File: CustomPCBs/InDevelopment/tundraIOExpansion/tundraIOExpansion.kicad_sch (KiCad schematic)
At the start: 35 parts, among them J1 Conn_01x25, J2 Conn_ARM_SWD_TagConnect_TC203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, U1 RP2040, U2 MX25L3233FM2, Y1 Crystal, Y2 32.768kHz

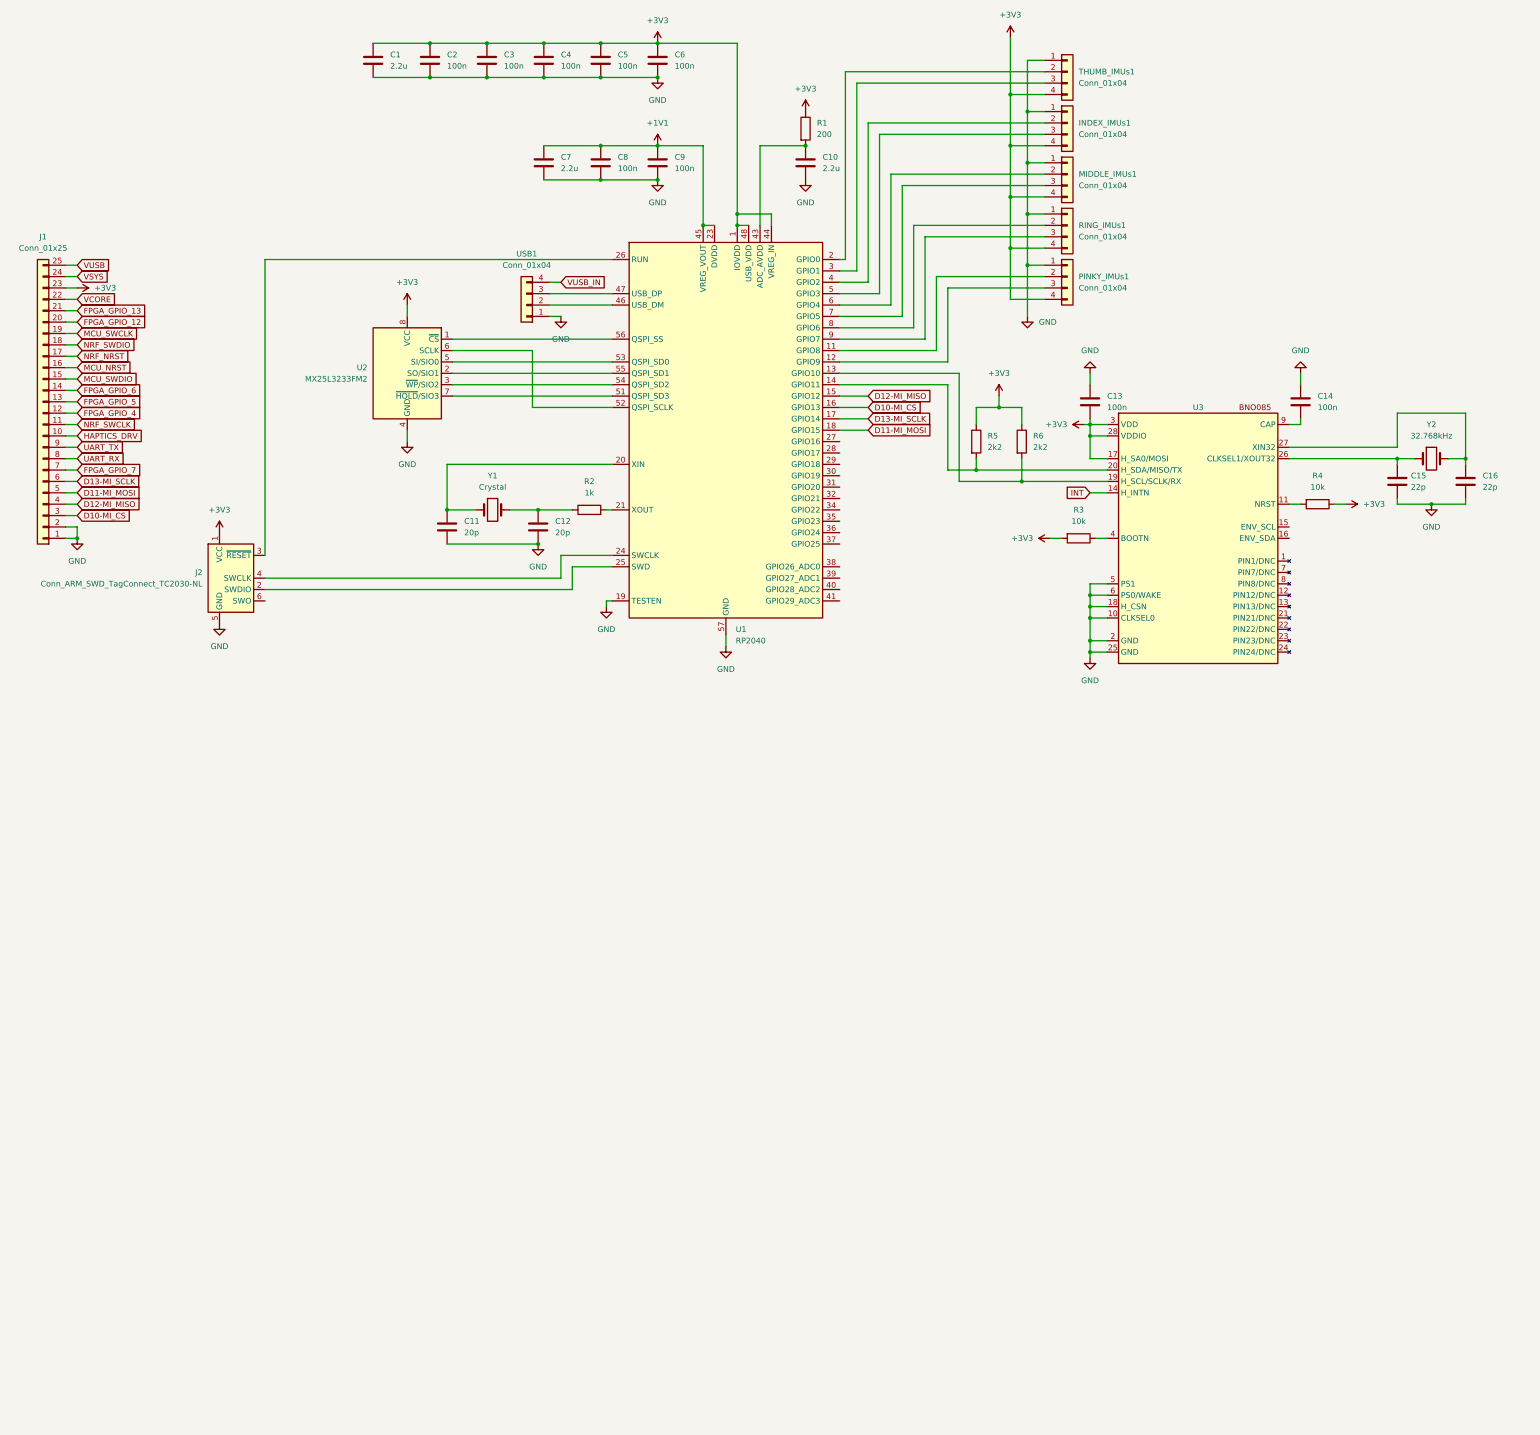
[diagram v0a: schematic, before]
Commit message: Adding variant for BNO 0x4A and 0x4B addresses
Also cleaned up the folder structure and changed schematic for the
custom Tundra expansion board
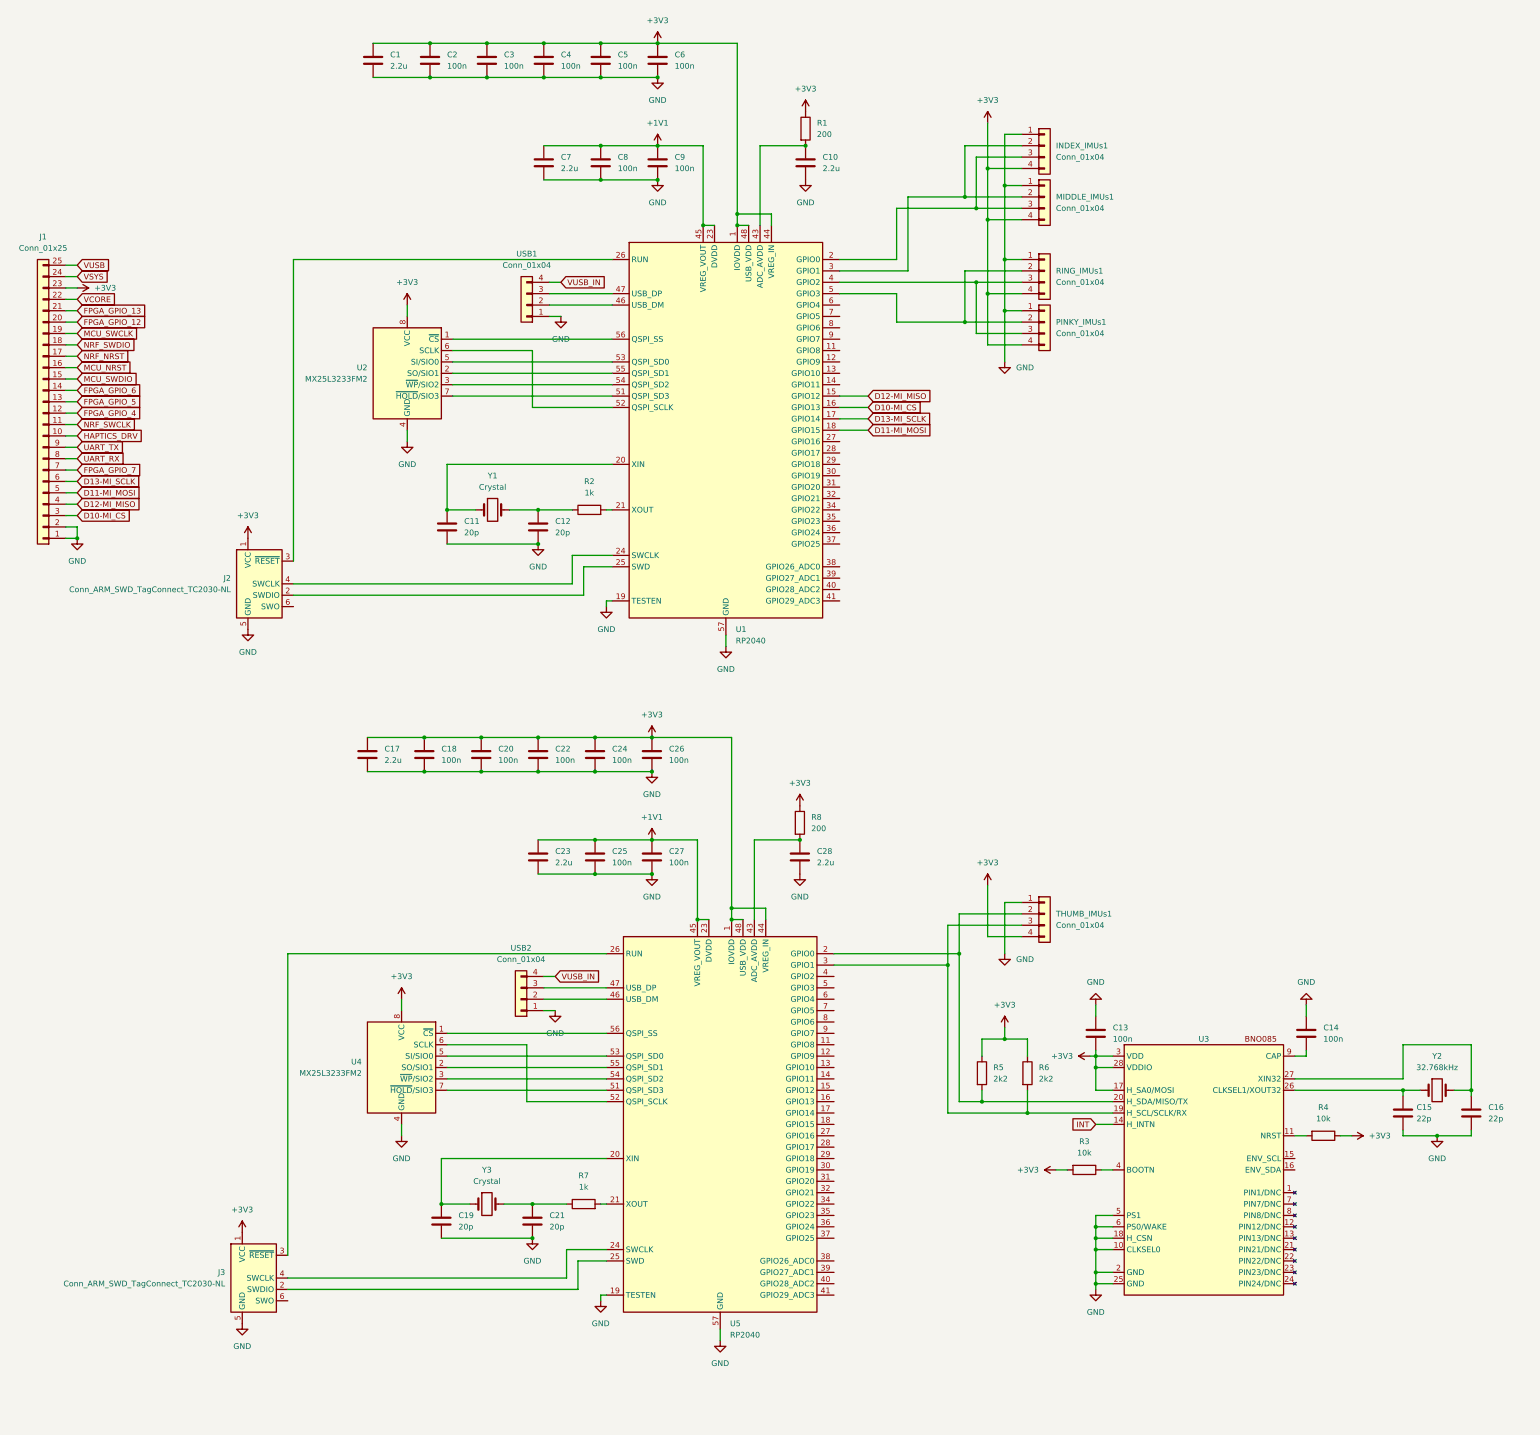
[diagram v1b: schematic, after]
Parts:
- added C17, C23, C28: 2.2u, Capacitor_SMD:C_0603_1608Metric, symbol Device:C
- added C18, C20, C22, C24, C25, C26, C27: 100n, Capacitor_SMD:C_0603_1608Metric, symbol Device:C
- added C19, C21: 20p, Capacitor_SMD:C_0603_1608Metric, symbol Device:C
- added J3: Conn_ARM_SWD_TagConnect_TC2030-NL, Connector:Tag-Connect_TC2030-IDC-NL_2x03_P1.27mm_Vertical, symbol Connector:Conn_ARM_SWD_TagConnect_TC2030-NL
- added R7: 1k, Resistor_SMD:R_0603_1608Metric, symbol Device:R
- added R8: 200, Resistor_SMD:R_0603_1608Metric, symbol Device:R
- added U4: MX25L3233FM2, Package_SO:SOP-8_5.28x5.23mm_P1.27mm, symbol Memory_Flash:MX25L3233FM2
- added U5: RP2040, Package_DFN_QFN:QFN-56-1EP_7x7mm_P0.4mm_EP3.2x3.2mm, symbol MCU_RaspberryPi:RP2040
- added USB2: Conn_01x04, Connector_JST:JST_SH_SM04B-SRSS-TB_1x04-1MP_P1.00mm_Horizontal, symbol Connector_Generic:Conn_01x04
- added Y3: Crystal, Crystal:Crystal_SMD_HC49-SD, symbol Device:Crystal
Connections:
- net +1V1: now also C23.1, C25.1, C27.1, U5.23 (DVDD), U5.45 (VREG_VOUT), U5.50 (DVDD)
- net +3V3: now also C17.1, C18.1, C20.1, C22.1, C24.1, C26.1, J3.1 (VCC), R8.1, U4.8 (VCC), U5.1 (IOVDD), U5.10 (IOVDD), U5.22 (IOVDD), U5.33 (IOVDD), U5.42 (IOVDD), U5.44 (VREG_IN), U5.48 (USB_VDD), U5.49 (IOVDD)
- net GND: now also C17.2, C18.2, C19.2, C20.2, C21.2, C22.2, C23.2, C24.2, C25.2, C26.2, C27.2, C28.2, J3.5 (GND), U4.4 (GND), U5.19 (TESTEN), U5.57 (GND), USB2.1 (Pin_1)
- net VUSB_IN: now also USB2.4 (Pin_4)
- net at R5.2, U3.20 (H_SDA/MISO/TX): now also THUMB_IMUs1.2 (Pin_2), U5.2 (GPIO0); no longer U1.14 (GPIO11)
- net at U1.11 (GPIO8): no longer PINKY_IMUs1.2 (Pin_2)
- net at U1.12 (GPIO9): no longer PINKY_IMUs1.3 (Pin_3)
- net at R6.2, U3.19 (H_SCL/SCLK/RX): now also THUMB_IMUs1.3 (Pin_3), U5.3 (GPIO1); no longer U1.13 (GPIO10)
- net at U1.2 (GPIO0): now also INDEX_IMUs1.3 (Pin_3), MIDDLE_IMUs1.3 (Pin_3); no longer THUMB_IMUs1.2 (Pin_2)
- net at U1.3 (GPIO1): now also INDEX_IMUs1.2 (Pin_2), MIDDLE_IMUs1.2 (Pin_2); no longer THUMB_IMUs1.3 (Pin_3)
- net at U1.4 (GPIO2): now also PINKY_IMUs1.3 (Pin_3), RING_IMUs1.3 (Pin_3); no longer INDEX_IMUs1.2 (Pin_2)
- net at U1.5 (GPIO3): now also PINKY_IMUs1.2 (Pin_2), RING_IMUs1.2 (Pin_2); no longer INDEX_IMUs1.3 (Pin_3)
- net at U1.6 (GPIO4): no longer MIDDLE_IMUs1.2 (Pin_2)
- net at U1.7 (GPIO5): no longer MIDDLE_IMUs1.3 (Pin_3)
- net at U1.8 (GPIO6): no longer RING_IMUs1.2 (Pin_2)
- net at U1.9 (GPIO7): no longer RING_IMUs1.3 (Pin_3)
- new net: J3.2 (SWDIO), U5.25 (SWD)
- new net: J3.3 (~{RESET}), U5.26 (RUN)
- new net: J3.4 (SWCLK), U5.24 (SWCLK)
- new net: C21.1, R7.1, Y3.2
- new net: R7.2, U5.21 (XOUT)
- new net: C19.1, U5.20 (XIN), Y3.1
- new net: C28.1, R8.2, U5.43 (ADC_AVDD)
- new net: U4.1 (~{CS}), U5.56 (QSPI_SS)
- new net: U4.2 (SO/SIO1), U5.55 (QSPI_SD1)
- new net: U4.3 (~{WP}/SIO2), U5.54 (QSPI_SD2)
- new net: U4.5 (SI/SIO0), U5.53 (QSPI_SD0)
- new net: U4.6 (SCLK), U5.52 (QSPI_SCLK)
- new net: U4.7 (~{HOLD}/SIO3), U5.51 (QSPI_SD3)
- new net: U5.46 (USB_DM), USB2.2 (Pin_2)
- new net: U5.47 (USB_DP), USB2.3 (Pin_3)
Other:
- moved on the sheet: C13, C14, C15, C16, INDEX_IMUs1, J2, MIDDLE_IMUs1, PINKY_IMUs1, R3, R4, R5, R6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

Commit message: Updating some footprints
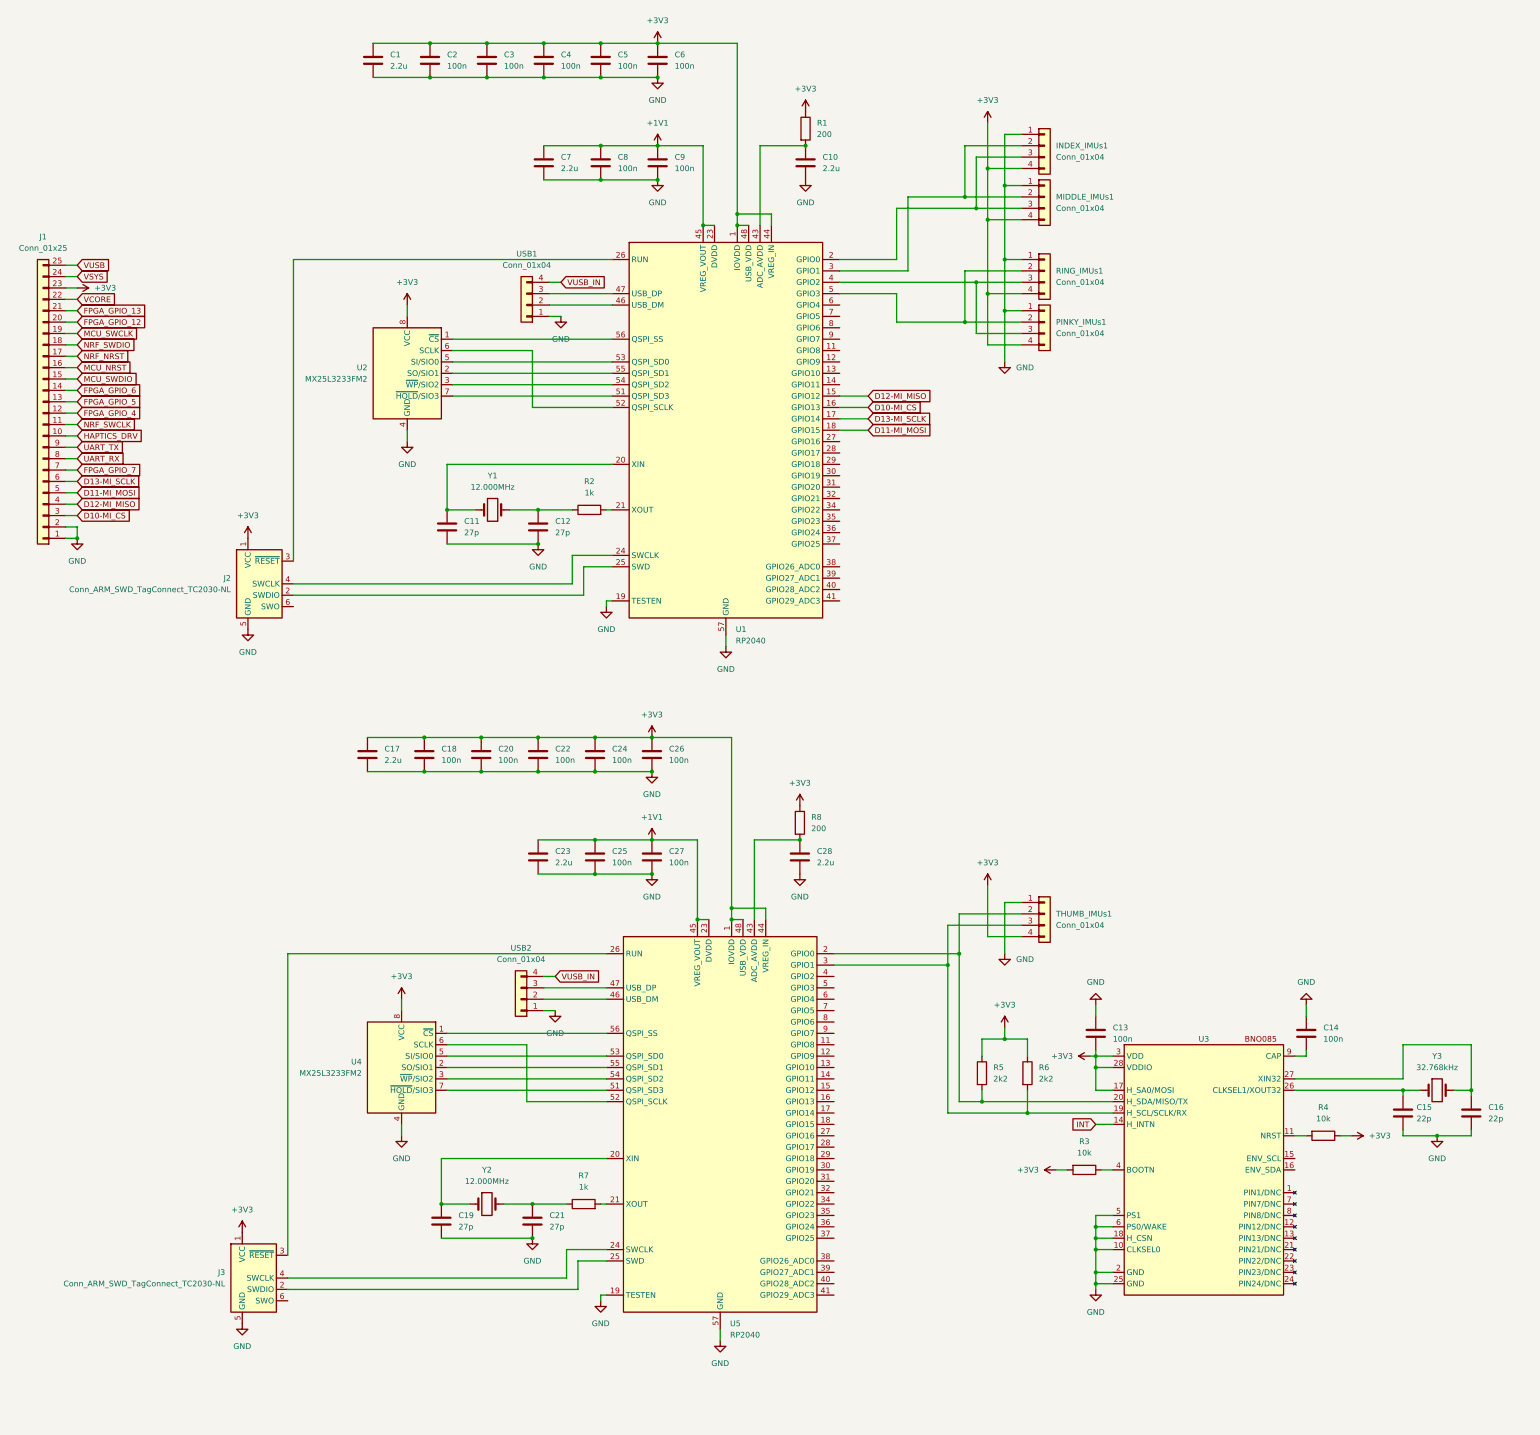
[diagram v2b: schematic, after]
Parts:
- removed Y3: Crystal, Crystal:Crystal_SMD_HC49-SD, symbol Device:Crystal
- added Y2: 12.000MHz, Crystal:Crystal_SMD_3225-4Pin_3.2x2.5mm, symbol Device:Crystal
- C1, C10, C13, C14, C15, C16, C17, C18, C2, C20, C22, C23, C24, C25, C26, C27, C28, C3, C4, C5, C6, C7, C8, C9: footprint Capacitor_SMD:C_0603_1608Metric -> Capacitor_SMD:C_0402_1005Metric
- C11, C12, C19, C21: value 20p -> 27p; footprint Capacitor_SMD:C_0603_1608Metric -> Capacitor_SMD:C_0402_1005Metric
- R1, R2, R3, R4, R5, R6, R7, R8: footprint Resistor_SMD:R_0603_1608Metric -> Resistor_SMD:R_0402_1005Metric
- Y1: value Crystal -> 12.000MHz; footprint Crystal:Crystal_SMD_HC49-SD -> Crystal:Crystal_SMD_3225-4Pin_3.2x2.5mm
- Y3: renamed from Y2; footprint Crystal:Crystal_SMD_3215-2Pin_3.2x1.5mm -> Crystal:Crystal_SMD_2012-2Pin_2.0x1.2mm
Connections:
- net at C21.1, R7.1: now also Y2.2
- net at C19.1, U5.20 (XIN): now also Y2.1

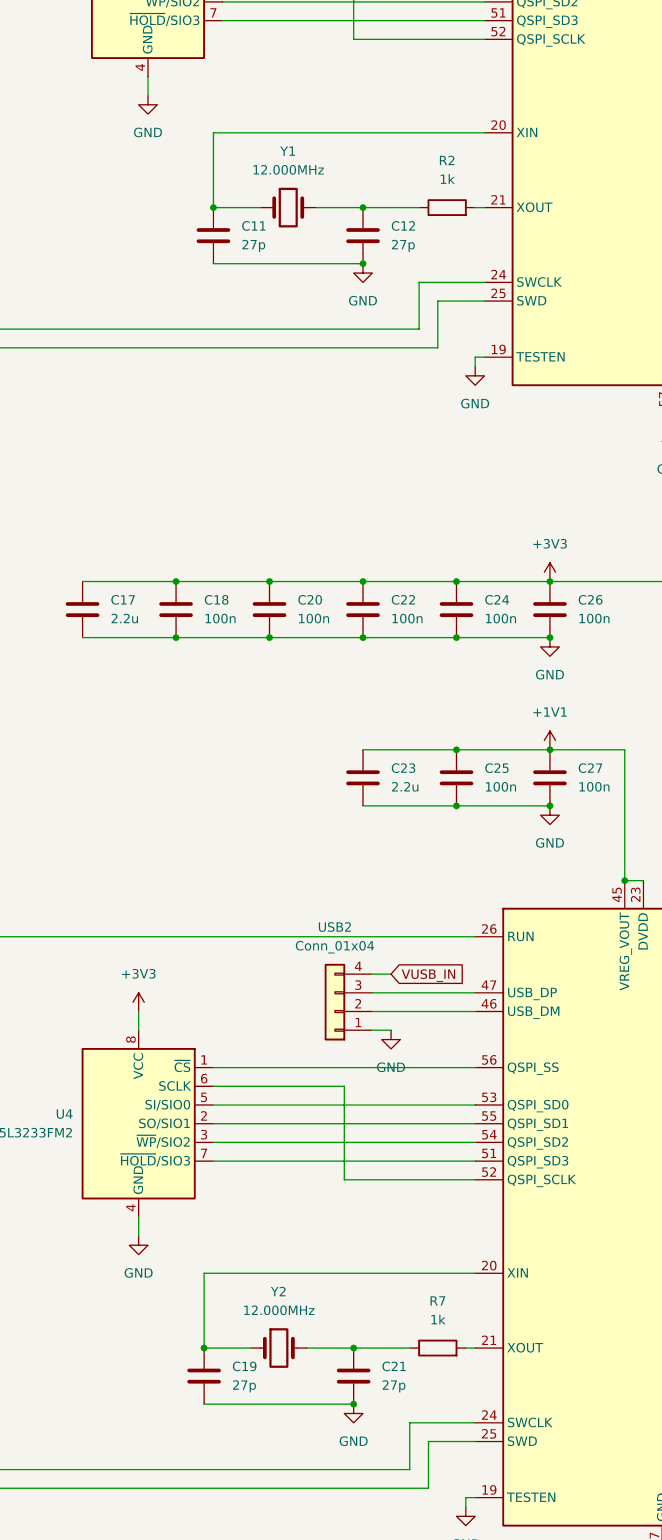
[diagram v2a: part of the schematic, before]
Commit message: Most components placed on tundra interface pcb
Decoupling caps next and then maybe adding some more connectors where
possible for future functionality expansion
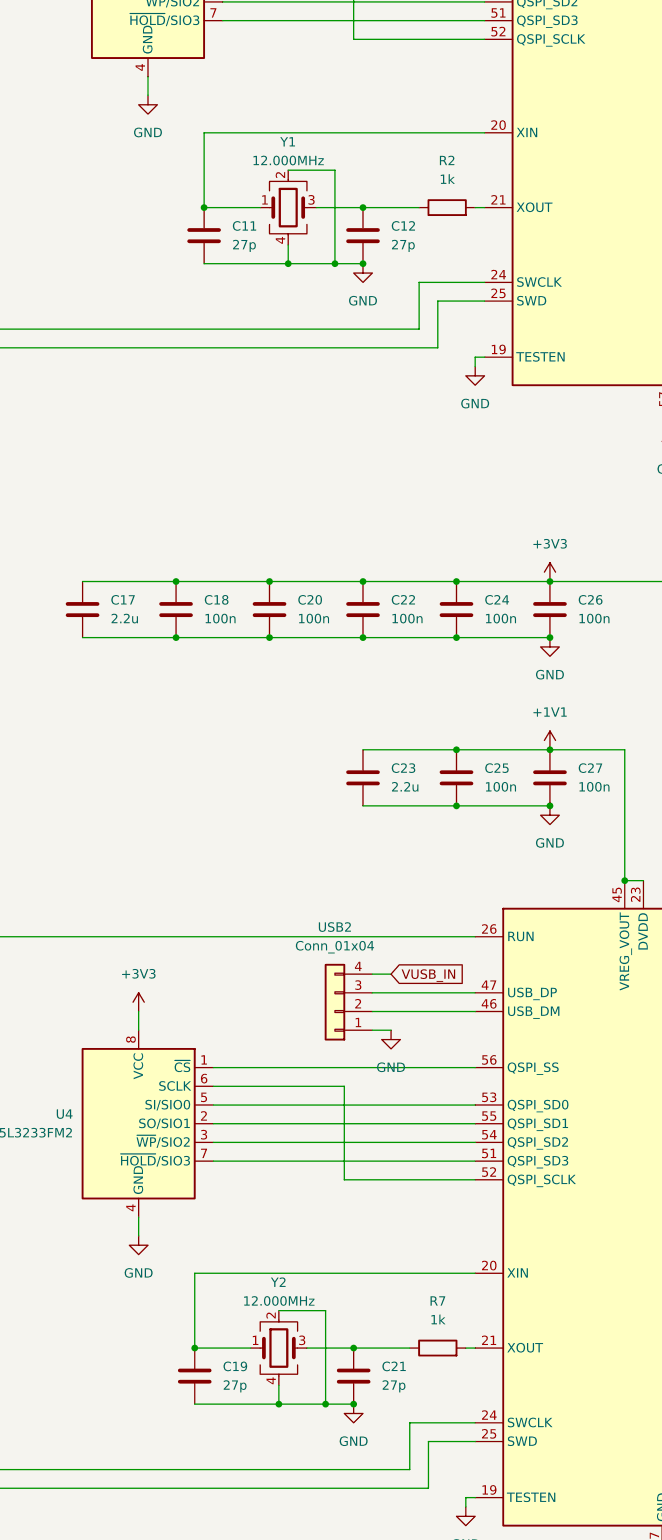
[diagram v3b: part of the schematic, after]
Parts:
- removed Y1, Y2: 12.000MHz, Crystal:Crystal_SMD_3225-4Pin_3.2x2.5mm, symbol Device:Crystal
- added Y1, Y2: 12.000MHz, Crystal:Crystal_SMD_3225-4Pin_3.2x2.5mm, symbol Device:Crystal_GND24
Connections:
- net GND: now also Y1.2, Y1.4, Y2.2, Y2.4
- net at C11.1, U1.20 (XIN): now also Y1.1
- net at C12.1, R2.1: now also Y1.3
- net at C21.1, R7.1: now also Y2.3
- net at C19.1, U5.20 (XIN): now also Y2.1
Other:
- moved on the sheet: C11, C19
